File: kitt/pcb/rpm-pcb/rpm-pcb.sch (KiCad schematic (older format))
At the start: 178 parts, among them J1 Screw_Terminal_01x02, J2 Screw_Terminal_01x02, Q1 NDP6020P, Q2 NDP6020P, Q3 NDP6020P, Q4 NDP6020P, Q5 NDP6020P, Q6 NDP6020P, U1 TLC5940NT, U2 TLC5940NT, U3 TLC5940NT, U4 TLC5940NT, U5 TLC5940NT, U6 TLC5940NT, U7 TLC5940NT, U8 TLC5940NT, U9 TLC5940NT

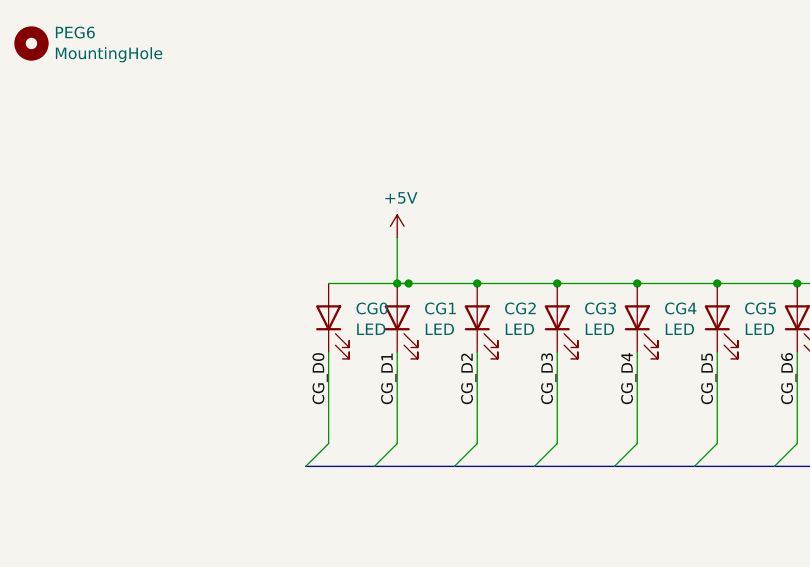
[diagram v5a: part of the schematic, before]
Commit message: fixed 12 seg leds
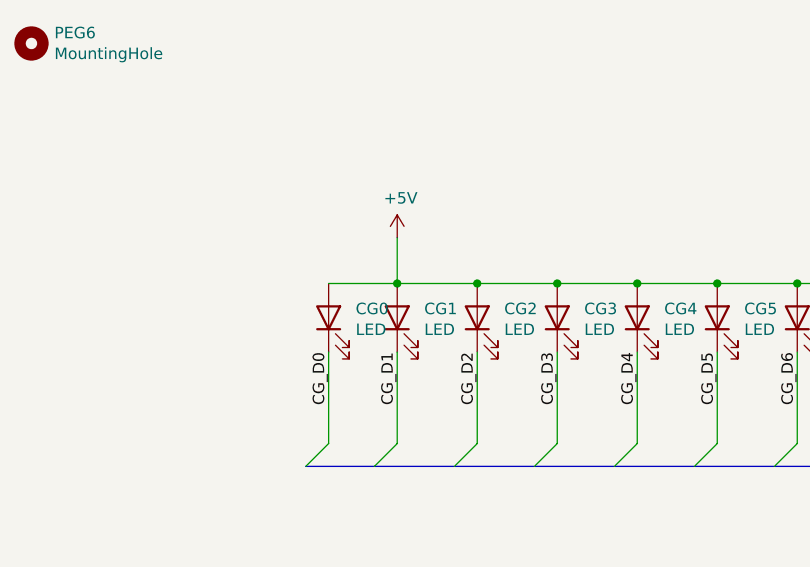
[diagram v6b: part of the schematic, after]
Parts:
- KEG_1_CAP_L1, KEG_1_CAP_R1, KEG_CAP_2_L1, KEG_CAP_2_R1, KEG_CAP_3_L1, KEG_CAP_3_R1, LAGER_1_T_L1, LAGER_2_T_L1, LAGER_3_T_L1: footprint KITT-Footpads:LED_12_Segment_2.0mm_24_pin -> KITT-Footpads:KYX_125807R
- KEG_1_T1, KEG_2_T1, KEG_3_T1, KEG_4_T1, KEG_5_T1, LAGER_1_T_R1, LAGER_2_T_R1, LAGER_3_T_R1, LINE_T1: footprint KITT-Footpads:LED_12_Segment_2.0mm_24_pin -> KITT-Footpads:STBD001_4R8G
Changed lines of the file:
@@
 F 0 "LAGER_2_T_R1" H 25578 5446 50  0000 L CNN
 F 1 "STBD01-4R8GA" H 25578 5355 50  0000 L CNN
-F 2 "KITT-Footpads:LED_12_Segment_2.0mm_24_pin" H 23800 5700 50  0001 C CNN
+F 2 "KITT-Footpads:STBD001_4R8G" H 23800 5700 50  0001 C CNN
 F 3 "" H 23800 5700 50  0001 C CNN
 	1    24750 5400
@@
 F 0 "LAGER_1_T_R1" H 25578 2796 50  0000 L CNN
 F 1 "STBD01-4R8GA" H 25578 2705 50  0000 L CNN
-F 2 "KITT-Footpads:LED_12_Segment_2.0mm_24_pin" H 23800 3050 50  0001 C CNN
+F 2 "KITT-Footpads:STBD001_4R8G" H 23800 3050 50  0001 C CNN
 F 3 "" H 23800 3050 50  0001 C CNN
 	1    24750 2750
@@
 F 0 "LINE_T1" H 9828 15596 50  0000 L CNN
 F 1 "STBD01-4R8GA" H 9828 15505 50  0000 L CNN
-F 2 "KITT-Footpads:LED_12_Segment_2.0mm_24_pin" H 8050 15850 50  0001 C CNN
+F 2 "KITT-Footpads:STBD001_4R8G" H 8050 15850 50  0001 C CNN
 F 3 "" H 8050 15850 50  0001 C CNN
 	1    9000 15550
@@
 F 0 "KEG_3_T1" H 7078 15596 50  0000 L CNN
 F 1 "STBD01-4R8GA" H 7078 15505 50  0000 L CNN
-F 2 "KITT-Footpads:LED_12_Segment_2.0mm_24_pin" H 5300 15850 50  0001 C CNN
+F 2 "KITT-Footpads:STBD001_4R8G" H 5300 15850 50  0001 C CNN
 F 3 "" H 5300 15850 50  0001 C CNN
 	1    6250 15550
@@
 F 0 "KEG_5_T1" H 9828 12346 50  0000 L CNN
 F 1 "STBD01-4R8GA" H 9828 12255 50  0000 L CNN
-F 2 "KITT-Footpads:LED_12_Segment_2.0mm_24_pin" H 8050 12600 50  0001 C CNN
+F 2 "KITT-Footpads:STBD001_4R8G" H 8050 12600 50  0001 C CNN
 F 3 "" H 8050 12600 50  0001 C CNN
 	1    9000 12300
@@
 F 0 "KEG_2_T1" H 7078 12346 50  0000 L CNN
 F 1 "STBD01-4R8GA" H 7078 12255 50  0000 L CNN
-F 2 "KITT-Footpads:LED_12_Segment_2.0mm_24_pin" H 5300 12600 50  0001 C CNN
+F 2 "KITT-Footpads:STBD001_4R8G" H 5300 12600 50  0001 C CNN
 F 3 "" H 5300 12600 50  0001 C CNN
 	1    6250 12300
@@
 F 0 "LAGER_1_T_L1" H 20650 2800 50  0000 L CNN
 F 1 "125807R" H 20800 2700 50  0000 L CNN
-F 2 "KITT-Footpads:LED_12_Segment_2.0mm_24_pin" H 21300 3050 50  0001 C CNN
+F 2 "KITT-Footpads:KYX_125807R" H 21300 3050 50  0001 C CNN
 F 3 "" H 21300 3050 50  0001 C CNN
 	1    22250 2750
@@
 F 0 "LAGER_2_T_L1" H 20650 5500 50  0000 L CNN
 F 1 "125807R" H 20800 5400 50  0000 L CNN
-F 2 "KITT-Footpads:LED_12_Segment_2.0mm_24_pin" H 21300 5700 50  0001 C CNN
+F 2 "KITT-Footpads:KYX_125807R" H 21300 5700 50  0001 C CNN
 F 3 "" H 21300 5700 50  0001 C CNN
 	1    22250 5400
@@
 F 0 "LAGER_3_T_L1" H 20650 8200 50  0000 L CNN
 F 1 "125807R" H 20800 8100 50  0000 L CNN
-F 2 "KITT-Footpads:LED_12_Segment_2.0mm_24_pin" H 21300 8450 50  0001 C CNN
+F 2 "KITT-Footpads:KYX_125807R" H 21300 8450 50  0001 C CNN
 F 3 "" H 21300 8450 50  0001 C CNN
 	1    22250 8150
@@
 F 0 "KEG_1_CAP_L1" H 23028 10696 50  0000 L CNN
 F 1 "125807R" H 23028 10605 50  0000 L CNN
-F 2 "KITT-Footpads:LED_12_Segment_2.0mm_24_pin" H 21250 10950 50  0001 C CNN
+F 2 "KITT-Footpads:KYX_125807R" H 21250 10950 50  0001 C CNN
 F 3 "" H 21250 10950 50  0001 C CNN
 	1    22200 10650
@@
 F 0 "KEG_1_CAP_R1" H 25778 10696 50  0000 L CNN
 F 1 "125807R" H 25778 10605 50  0000 L CNN
-F 2 "KITT-Footpads:LED_12_Segment_2.0mm_24_pin" H 24000 10950 50  0001 C CNN
+F 2 "KITT-Footpads:KYX_125807R" H 24000 10950 50  0001 C CNN
 F 3 "" H 24000 10950 50  0001 C CNN
 	1    24950 10650
@@
 F 0 "KEG_CAP_2_L1" H 23078 13146 50  0000 L CNN
 F 1 "125807R" H 23078 13055 50  0000 L CNN
-F 2 "KITT-Footpads:LED_12_Segment_2.0mm_24_pin" H 21300 13400 50  0001 C CNN
+F 2 "KITT-Footpads:KYX_125807R" H 21300 13400 50  0001 C CNN
 F 3 "" H 21300 13400 50  0001 C CNN
 	1    22250 13100
@@
 F 0 "KEG_CAP_3_L1" H 23078 15596 50  0000 L CNN
 F 1 "125807R" H 23078 15505 50  0000 L CNN
-F 2 "KITT-Footpads:LED_12_Segment_2.0mm_24_pin" H 21300 15850 50  0001 C CNN
+F 2 "KITT-Footpads:KYX_125807R" H 21300 15850 50  0001 C CNN
 F 3 "" H 21300 15850 50  0001 C CNN
 	1    22250 15550
@@
 F 0 "KEG_CAP_3_R1" H 25828 15596 50  0000 L CNN
 F 1 "125807R" H 25828 15505 50  0000 L CNN
-F 2 "KITT-Footpads:LED_12_Segment_2.0mm_24_pin" H 24050 15850 50  0001 C CNN
+F 2 "KITT-Footpads:KYX_125807R" H 24050 15850 50  0001 C CNN
 F 3 "" H 24050 15850 50  0001 C CNN
 	1    25000 15550
@@
 F 0 "KEG_CAP_2_R1" H 25828 13146 50  0000 L CNN
 F 1 "125807R" H 25828 13055 50  0000 L CNN
-F 2 "KITT-Footpads:LED_12_Segment_2.0mm_24_pin" H 24050 13400 50  0001 C CNN
+F 2 "KITT-Footpads:KYX_125807R" H 24050 13400 50  0001 C CNN
 F 3 "" H 24050 13400 50  0001 C CNN
 	1    25000 13100
@@
 F 0 "KEG_4_T1" H 9828 9196 50  0000 L CNN
 F 1 "STBD01-4R8GA" H 9828 9105 50  0000 L CNN
-F 2 "KITT-Footpads:LED_12_Segment_2.0mm_24_pin" H 8050 9450 50  0001 C CNN
+F 2 "KITT-Footpads:STBD001_4R8G" H 8050 9450 50  0001 C CNN
 F 3 "" H 8050 9450 50  0001 C CNN
 	1    9000 9150
@@
 F 0 "KEG_1_T1" H 7078 9196 50  0000 L CNN
 F 1 "STBD01-4R8GA" H 7078 9105 50  0000 L CNN
-F 2 "KITT-Footpads:LED_12_Segment_2.0mm_24_pin" H 5300 9450 50  0001 C CNN
+F 2 "KITT-Footpads:STBD001_4R8G" H 5300 9450 50  0001 C CNN
 F 3 "" H 5300 9450 50  0001 C CNN
 	1    6250 9150
@@
 F 0 "LAGER_3_T_R1" H 25578 8196 50  0000 L CNN
 F 1 "STBD01-4R8GA" H 25578 8105 50  0000 L CNN
-F 2 "KITT-Footpads:LED_12_Segment_2.0mm_24_pin" H 23800 8450 50  0001 C CNN
+F 2 "KITT-Footpads:STBD001_4R8G" H 23800 8450 50  0001 C CNN
 F 3 "" H 23800 8450 50  0001 C CNN
 	1    24750 8150
@@
 Wire Wire Line
 	4450 3650 4750 3650
-Connection ~ 4800 3650
-Wire Wire Line
-	4800 3650 4750 3650
 Entry Wire Line
 	8000 16700 8100 16800
 Wire Wire Line
 	8100 16800 8100 17600
+Text Label 8100 17600 1    50   ~ 0
+CG_D0
 Wire Wire Line
 	4750 3650 5100 3650
@@
 Wire Bus Line
 	5400 16700 17300 16700
-Text Label 8100 17600 1    50   ~ 0
-CG_D0
 $EndSCHEMATC

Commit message: 220 tab down
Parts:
- Q4, Q5, Q6: footprint Package_TO_SOT_THT:TO-220-3_Vertical -> Package_TO_SOT_THT:TO-220-3_Horizontal_TabDown
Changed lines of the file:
@@
 F 0 "Q5" H 21005 3796 50  0000 L CNN
 F 1 "NDP6020P" H 21005 3705 50  0000 L CNN
-F 2 "Package_TO_SOT_THT:TO-220-3_Vertical" H 21000 3675 50  0001 L CIN
+F 2 "Package_TO_SOT_THT:TO-220-3_Horizontal_TabDown" H 21000 3675 50  0001 L CIN
 F 3 "https://www.onsemi.com/pdf/datasheet/ndp6020p-d.pdf" H 20800 3750 50  0001 L CNN
 	1    20800 3750
@@
 F 0 "Q6" H 21005 6546 50  0000 L CNN
 F 1 "NDP6020P" H 21005 6455 50  0000 L CNN
-F 2 "Package_TO_SOT_THT:TO-220-3_Vertical" H 21000 6425 50  0001 L CIN
+F 2 "Package_TO_SOT_THT:TO-220-3_Horizontal_TabDown" H 21000 6425 50  0001 L CIN
 F 3 "https://www.onsemi.com/pdf/datasheet/ndp6020p-d.pdf" H 20800 6500 50  0001 L CNN
 	1    20800 6500
@@
 F 0 "Q4" H 21005 1146 50  0000 L CNN
 F 1 "NDP6020P" H 21005 1055 50  0000 L CNN
-F 2 "Package_TO_SOT_THT:TO-220-3_Vertical" H 21000 1025 50  0001 L CIN
+F 2 "Package_TO_SOT_THT:TO-220-3_Horizontal_TabDown" H 21000 1025 50  0001 L CIN
 F 3 "https://www.onsemi.com/pdf/datasheet/ndp6020p-d.pdf" H 20800 1100 50  0001 L CNN
 	1    20800 1100

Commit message: fixed labels
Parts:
- removed R10, R12, R2, R4, R6, R8: 120R, Resistor_THT:R_Axial_DIN0207_L6.3mm_D2.5mm_P10.16mm_Horizontal, symbol Device:R
- R1: value 120R -> 22R
- R2: renamed from R3; value 120R -> 22R
- R3: renamed from R5; value 120R -> 22R
- R4: renamed from R7; value 120R -> 22R
- R5: renamed from R9; value 120R -> 22R
- R6: renamed from R11; value 120R -> 22R
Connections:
- net GND: no longer RPM1.1 (D1C), RPM1.5 (D3C), RPM2.1 (D1C), RPM2.5 (D3C), RPM3.1 (D1C), RPM3.5 (D3C)
- net at RPM1.3 (D2A): now also RPM1.1 (D1C)
- net at RPM1.7 (D4A): now also RPM1.5 (D3C)
- net at RPM2.3 (D2A): now also RPM2.1 (D1C)
- net at RPM2.7 (D4A): now also RPM2.5 (D3C)
- net at RPM3.7 (D4A): now also RPM3.5 (D3C)
- net at RPM3.3 (D2A): now also RPM3.1 (D1C)
